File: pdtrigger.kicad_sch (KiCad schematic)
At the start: 0 parts

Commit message: Initial ICs and passives
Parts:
- added C1: 100n, Capacitor_SMD:C_0402_1005Metric, symbol Device:C
- added C10, C11: 10p, Capacitor_SMD:C_0402_1005Metric, symbol Device:C
- added C2: 4.7u, Capacitor_SMD:C_0603_1608Metric, symbol Device:C
- added D1: RED, LED_SMD:LED_0805_2012Metric, symbol Device:LED
- added J2: USB_C_Receptacle_USB2.0_16P, libs:USB-C-SMD_TYPE-C-6PIN-2MD-073, symbol Connector:USB_C_Receptacle_USB2.0_16P
- added R1: 2k2, Resistor_SMD:R_0603_1608Metric, symbol Device:R
- added U1: STM32F401RBT6, Package_QFP:LQFP-64_10x10mm_P0.5mm, symbol MCU_ST_STM32F4:STM32F401RBTx
- added U2: CYPD3177-24LQXQ_C2959321, libs:TQFN-24_L4.0-W4.0-P0.50-TL-EP2.8, symbol libs:CYPD3177-24LQXQ_C2959321
- added Y1: 16MHz, libs:OSC-SMD_4P-L3.2-W2.5-BL, symbol Device:Crystal_GND24
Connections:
- new net: R1.1, U1.26 (PB0)
- new net: D1.2 (A), R1.2
- new net: J2.A4 (VBUS), J2.A9 (VBUS), J2.B4 (VBUS), J2.B9 (VBUS)
- new net GND: C1.2, C10.2, C11.2, C2.2, D1.1 (K), J2.A1 (GND), J2.A12 (GND), J2.B1 (GND), J2.B12 (GND), J2.S1 (SHIELD), U1.12 (VSSA), U1.18 (VSS), U1.31 (VSS), U1.47 (VSS), U1.63 (VSS), Y1.2, Y1.4
- new net HSE_IN: C10.1, U1.5 (PH0), Y1.1
- new net HSE_OUT: C11.1, U1.6 (PH1), Y1.3
- new net I2C3_SDA: U1.40 (PC9)
- new net NRST: C1.1, U1.7 (NRST)
- new net PD_GPIO: U1.50 (PA15)
- new net PD_INT: U1.52 (PC11)
- new net PD_SAFE: U1.53 (PC12)
- new net SWCLK: U1.49 (PA14)
- new net SWDIO: U1.46 (PA13)
- new net USB_D+: J2.A6 (D+), J2.B6 (D+), U1.45 (PA12)
- new net USB_D-: J2.A7 (D-), J2.B7 (D-), U1.44 (PA11)
- new net VCAP1: C2.1, U1.30 (VCAP1)
- no-connect marks 0 -> 4
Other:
- note added: "C_load = 2*(C_LO - C_S) = 2*(9-4) = 10pF"

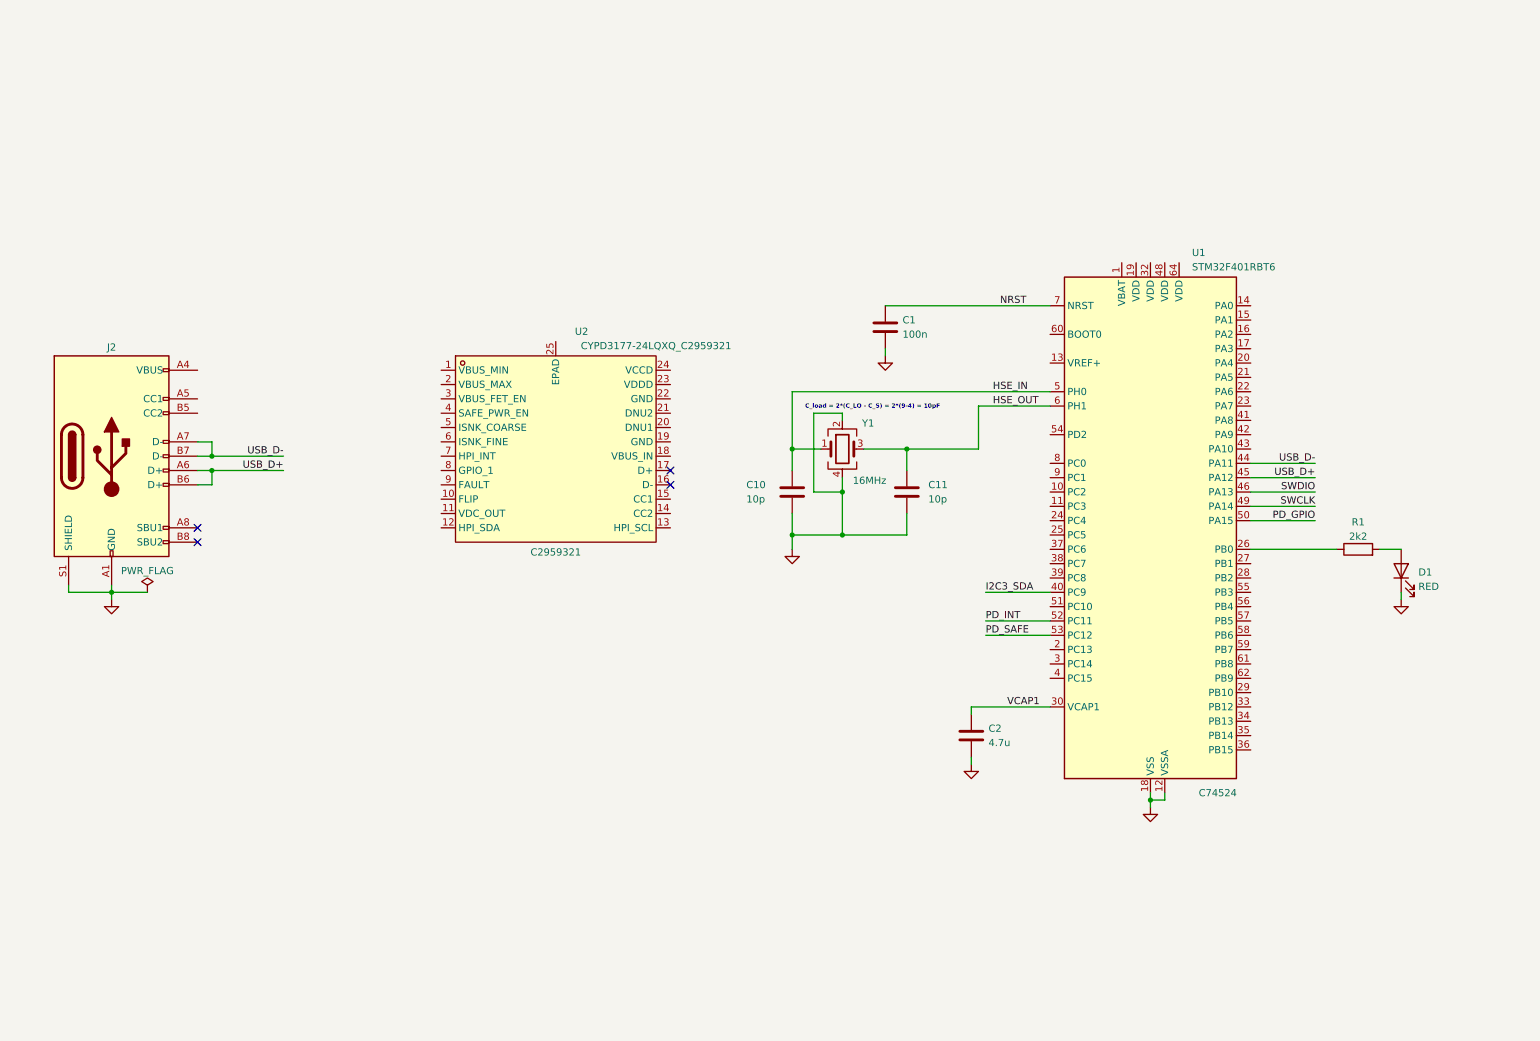
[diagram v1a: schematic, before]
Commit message: 70% finished with component selection and schem entry
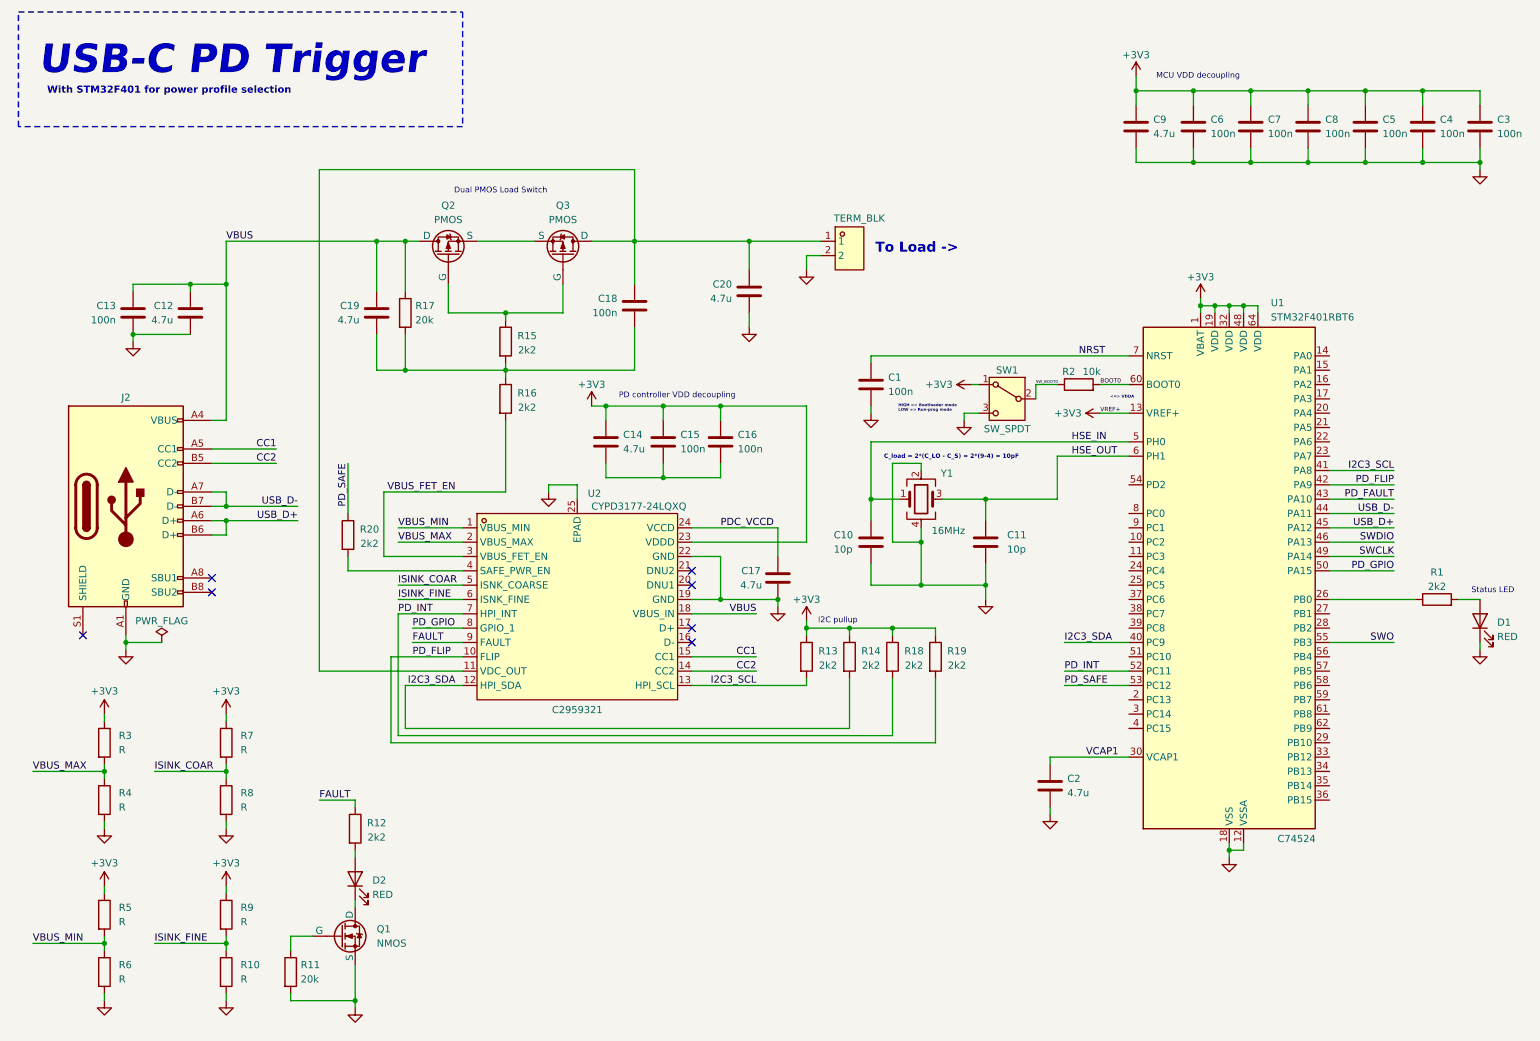
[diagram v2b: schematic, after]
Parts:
- added C12, C14, C17, C19, C20, C9: 4.7u, Capacitor_SMD:C_0603_1608Metric, symbol Device:C
- added C13, C15, C16, C18, C3, C4, C5, C6, C7, C8: 100n, Capacitor_SMD:C_0402_1005Metric, symbol Device:C
- added D2: RED, LED_SMD:LED_0805_2012Metric, symbol Device:LED
- added Q1: NMOS, symbol Simulation_SPICE:NMOS
- added Q2, Q3: PMOS, libs:SO-8_L4.9-W3.9-P1.27-LS5.9-BL, symbol Simulation_SPICE:PMOS
- added R10, R3, R4, R5, R6, R7, R8, R9: R, symbol Device:R
- added R11, R17: 20k, Resistor_SMD:R_0603_1608Metric, symbol Device:R
- added R12, R13, R14, R15, R16, R18, R19, R20: 2k2, Resistor_SMD:R_0603_1608Metric, symbol Device:R
- added R2: 10k, Capacitor_SMD:C_0402_1005Metric, symbol Device:R
- added SW1: SW_SPDT, libs:SW-SMD_K3-1280S-K1, symbol Switch:SW_SPDT
- added U3: TERM_BLK, libs:CONN-TH_P5.00_KF301-5.0-2P, symbol libs:KF301-5.0-2P
- U2: value CYPD3177-24LQXQ_C2959321 -> CYPD3177-24LQXQ
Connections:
- net GND: now also U2.19 (GND), U2.22 (GND), U2.25 (EPAD), C12.2, C13.2, C17.1, C20.2, C3.2, C4.2, C5.2, C6.2, C7.2, C8.2, C9.2, Q1.3 (S), R10.2, R11.2, R4.2, R6.2, R8.2, SW1.3 (C), U3.2; no longer J2.S1 (SHIELD)
- net I2C3_SDA: now also U2.12 (HPI_SDA), R14.2
- net PD_GPIO: now also U2.8 (GPIO_1)
- net PD_INT: now also U2.7 (HPI_INT), R18.2
- net PD_SAFE: now also R20.1
- net VBUS_MIN: now reaches U2.1 (VBUS_MIN)
- net VBUS_MIN: now also R5.2, R6.1
- net PD_FLIP: now reaches U2.10 (FLIP)
- net PD_FLIP: now also U1.42 (PA9), R19.2
- net at U2.11 (VDC_OUT): now also C18.1, C20.1, Q3.1 (D), U3.1
- net I2C3_SCL: now reaches U2.13 (HPI_SCL)
- net I2C3_SCL: now also U1.41 (PA8), R13.2
- net CC2: now reaches U2.14 (CC2)
- net CC2: now also J2.B5 (CC2)
- net CC1: now reaches U2.15 (CC1)
- net CC1: now also J2.A5 (CC1)
- net VBUS: now reaches U2.18 (VBUS_IN)
- net VBUS: now also J2.A4 (VBUS), J2.A9 (VBUS), J2.B4 (VBUS), J2.B9 (VBUS), C12.1, C13.1, C19.1, Q2.1 (D), R17.1
- net VBUS_MAX: now reaches U2.2 (VBUS_MAX)
- net VBUS_MAX: now also R3.2, R4.1
- net +3V3: now reaches U2.23 (VDDD)
- net +3V3: now also U1.1 (VBAT), U1.13 (VREF+), U1.19 (VDD), U1.32 (VDD), U1.48 (VDD), U1.64 (VDD), C14.1, C15.1, C16.1, C3.1, C4.1, C5.1, C6.1, C7.1, C8.1, C9.1, R13.1, R14.1, R18.1, R19.1, R3.1, R5.1, R7.1, R9.1, SW1.1 (A)
- net PDC_VCCD: now reaches U2.24 (VCCD)
- net PDC_VCCD: now also C17.2
- net VBUS_FET_EN: now reaches U2.3 (VBUS_FET_EN)
- net VBUS_FET_EN: now also R16.2
- net at U2.4 (SAFE_PWR_EN): now also R20.2
- net ISINK_COAR: now reaches U2.5 (ISNK_COARSE)
- net ISINK_COAR: now also R7.2, R8.1
- net ISINK_FINE: now reaches U2.6 (ISNK_FINE)
- net ISINK_FINE: now also R10.1, R9.2
- net FAULT: now reaches U2.9 (FAULT)
- net FAULT: now also R12.1
- net PD_FAULT: now reaches U1.43 (PA10)
- net SWO: now reaches U1.55 (PB3)
- net BOOT0: now reaches U1.60 (BOOT0)
- net BOOT0: now also R2.2
- new net: C18.2, C19.2, R15.2, R16.1, R17.2
- new net: Q1.2 (G), R11.1
- new net: C14.2, C15.2, C16.2
- new net: D2.1 (K), Q1.1 (D)
- new net: D2.2 (A), R12.2
- new net: Q2.2 (G), Q3.2 (G), R15.1
- new net: Q2.3 (S), Q3.3 (S)
- new net SW_BOOT0: R2.1, SW1.2 (B)
- no-connect marks 4 -> 7
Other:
- note added: "<=> VDDA"
- note added: "Dual PMOS Load Switch"
- note added: "HIGH => Bootloader mode LOW => Run-prog mode"
- note added: "I2C pullup"
- note added: "MCU VDD decoupling"
- note added: "PD controller VDD decoupling"
- note added: "Status LED"
- note added: "To Load ->"
- note added: "USB-C PD Trigger"
- note added: "With STM32F401 for power profile selection"
- company: (none) -> Lachlan Cooke
- title: (none) -> USB-C PD Trigger
- moved on the sheet: C1, C10, C11, C2, D1, J2, R1, U1, U2, Y1

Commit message: Final wiring before leaving office
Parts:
- added C21, C23, C24: 4.7u, Capacitor_SMD:C_0603_1608Metric, symbol Device:C
- added C22: 100n, Capacitor_SMD:C_0402_1005Metric, symbol Device:C
- added C25: 10p, Capacitor_SMD:C_0402_1005Metric, symbol Device:C
- added L1: 47u, symbol Device:L
- added R21, R22, R23, R24, R25: 20k, Resistor_SMD:R_0603_1608Metric, symbol Device:R
- added R26: 2k2, Resistor_SMD:R_0603_1608Metric, symbol Device:R
- added U4: SY8303AIC, libs:TSOT-23-8_L2.9-W1.6-P0.65-LS2.8-BR, symbol libs:SY8303AIC
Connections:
- net +3V3: now also C23.1, C24.1, C25.1, L1.2, R24.1, R25.1
- net GND: now also C21.2, C23.2, C24.2, R23.2, R26.2, U4.3 (GND), U4.4 (GND)
- net VBUS: now also C21.1, R21.1, U4.5 (IN)
- net SAFE_PWR_EN: now reaches R20.2, U2.4 (SAFE_PWR_EN)
- new net: R22.2, R23.1
- new net: R21.2, U4.8 (EN)
- new net: C22.2, L1.1, U4.6 (LX)
- new net: C22.1, U4.7 (BS)
- new net BUCK_FB: C25.2, R24.2, R25.2, R26.1, U4.1 (FB)
- new net BUCK_FS: R22.1, U4.2 (FS)
- no-connect marks 7 -> 42
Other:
- note added: "<- change PAD NO.s!"
- note added: "V_out = 0.6*(1 + Rhi/Rlo) = 0.6*(1 + 10/2.2) = 3.33 V"
- moved on the sheet: C12, C13, D2, Q1, R10, R11, R12, R3, R4, R5, R6, R7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
